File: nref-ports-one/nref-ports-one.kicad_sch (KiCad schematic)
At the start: 91 parts, among them J1 CONN_HEAD, J10 CONN_SPK, J2 DM3AT-SF-PEJM5, J3 09452812561, J4 USB_C_Receptacle, J5 Conn_01x10_Pin, J6 Conn_01x14_Pin, J7 Conn_01x12_Pin, J8 PWR, J9 Conn_01x10_Pin, U1 TPS7A0533PDBZ, U2 TLV320AIC3100, U3 TXS0108EPW, U4 SN74AVC1T45, U5 TPD4E02B04DQA, U6 TPD4E02B04DQA, U7 TPD4E02B04DQA, U8 FUSB302BMPX, U9 AP22815A

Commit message: ports one: some routing
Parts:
- removed FB5, FB6: 100@100MHz 3A, Inductor_SMD:L_0603_1608Metric, symbol Device:FerriteBead_Small
- C25: footprint Capacitor_SMD:C_0603_1608Metric -> Capacitor_SMD:C_0402_1005Metric
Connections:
- net GND: no longer J8.1 (Pin_1), J8.2 (Pin_2)
- net GNDA: no longer C24.1, C25.2, J10.2 (Pin_2), L2.2
- new net: C24.1, C25.2, J10.2 (Pin_2), L2.2
- new net VCC: J8.1 (Pin_1), J8.2 (Pin_2)
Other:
- note added: "TODO"
- moved on the sheet: C23, C24

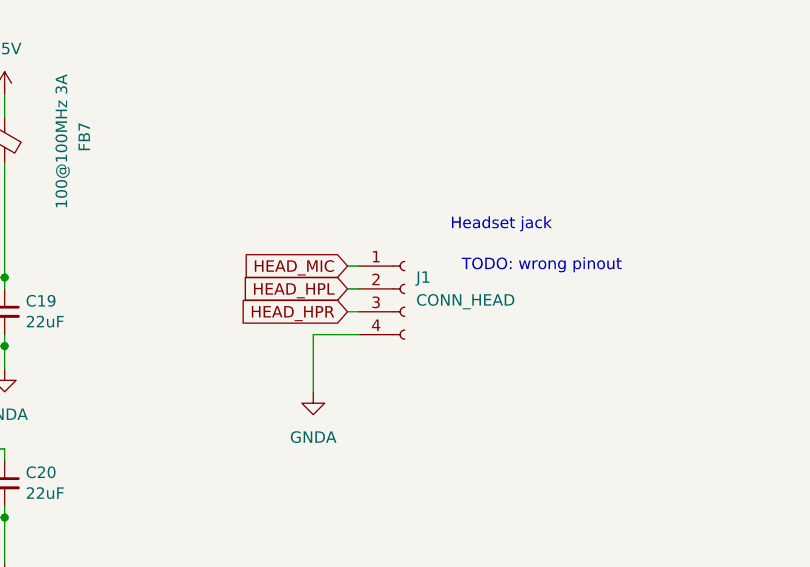
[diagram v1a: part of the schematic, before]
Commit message: ports 1 routing, ports 2 location tweaks
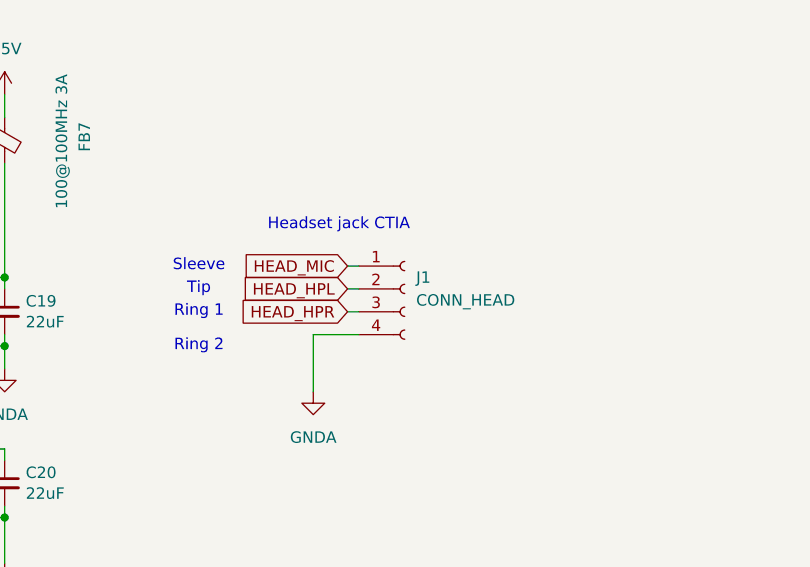
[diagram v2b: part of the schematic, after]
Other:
- note added: "Headset jack CTIA"
- note added: "Ring 1"
- note added: "Ring 2"
- note added: "Sleeve"
- note added: "Tip"
- note removed: "Headset jack"
- note removed: "TODO: wrong pinout"
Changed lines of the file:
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@@
-		)
-	)
-	(text "TODO: wrong pinout"
-		(exclude_from_sim no)
-		(at 198.12 393.7 0)
-		(effects
-			(font
-				(size 1.27 1.27)
-			)
 		)
 	)
@@
 		)
 	)
+	(text "Ring 1"
+		(exclude_from_sim no)
+		(at 160.02 398.78 0)
+		(effects
+			(font
+				(size 1.27 1.27)
+			)
+		)
+	)
 	(text "Audio"
 		(exclude_from_sim no)
@@
 			)
 			(justify left bottom)
+		)
+	)
+	(text "Sleeve"
+		(exclude_from_sim no)
+		(at 160.02 393.7 0)
+		(effects
+			(font
+				(size 1.27 1.27)
+			)
 		)
 	)
@@
 		)
 	)
-	(text "Headset jack"
+	(text "Headset jack CTIA"
 		(exclude_from_sim no)
-		(at 187.96 389.89 0)
+		(at 167.64 389.89 0)
 		(effects
 			(font
@@
 			)
 			(justify left bottom)
+		)
+	)
+	(text "Tip"
+		(exclude_from_sim no)
+		(at 160.02 396.24 0)
+		(effects
+			(font
+				(size 1.27 1.27)
+			)
 		)
 	)
@@
 		)
 	)
+	(text "Ring 2"
+		(exclude_from_sim no)
+		(at 160.02 402.59 0)
+		(effects
+			(font
+				(size 1.27 1.27)
+			)
+		)
+	)

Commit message: ports one: more design and more routing
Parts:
- added C38, C39, C40: 47uF, Capacitor_SMD:C_1206_3216Metric, symbol Device:C_Small
- added C41, C42: 0.1uF, Capacitor_SMD:C_0402_1005Metric, symbol Device:C_Small
- added C43, C44: 1uF, Capacitor_SMD:C_0402_1005Metric, symbol Device:C_Small
- added R20, R21, R22, R24, R31, R32, R33: 0, Resistor_SMD:R_0402_1005Metric, symbol Device:R_Small
- added R23, R25, R26, R27, R30: 200k, Resistor_SMD:R_0402_1005Metric, symbol Device:R_Small
- added R28, R34: 10k, Resistor_SMD:R_0402_1005Metric, symbol Device:R_Small
- added R29: 900k, Resistor_SMD:R_0402_1005Metric, symbol Device:R_Small
- added U10: HD3SS3220IRNHT, footprints:QFN40P450X250X80-31N120X320, symbol HD3SS3220IRNHT:HD3SS3220IRNHT
- added U11: PCAL6416AHF, Package_DFN_QFN:HVQFN-24-1EP_4x4mm_P0.5mm_EP2.1x2.1mm, symbol Interface_Expansion:PCAL6416AHF
- added U12: TLV75518PDBV, Package_TO_SOT_SMD:SOT-23-5, symbol Regulator_Linear:TLV75518PDBV
- J1: footprint (none) -> footprints:CUI_SJ-43614-SMT
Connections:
- net USBH_2_DN is gone; now on net USB1_DN: J4.A7 (D-), J4.B7 (D-), U5.4 (IO3), U5.7 (IO3)
- net USBH_2_DP is gone; now on net USB1_DP: J4.A6 (D+), J4.B6 (D+), U5.5 (IO4), U5.6 (IO4)
- net VCHG is gone; now on net VPD: D3.1 (K)
- net +1V8: now also C44.1, U12.5 (OUT)
- net +3V3: now also C43.1, R22.2, U12.1 (IN), U12.3 (EN)
- net +5V: now also R24.2
- net GND: now also C38.2, C39.2, C40.2, C41.2, C42.2, C43.2, C44.2, R31.1, U10.13 (GND), U10.22 (ADDR), U10.28 (GND), U10.29 (~{ENN_CC}), U10.31 (EXP_PAD), U11.18 (ADDR), U11.25 (EP), U11.9 (V_{SS}), U12.2 (GND)
- net RP_FUSB_INT: now also U11.8 (P0_7)
- net RP_SCL0: now also R32.2, U11.19 (SCL)
- net RP_SDA0: now also R33.2, U11.20 (SDA)
- net STANDBY_3V3: now also C41.1, R34.1, U11.21 (V_{DD(P)}), U11.23 (V_{DD(I2C-bus)})
- net USB1_RXN: now also U10.10 (RXN)
- net USB1_RXP: now also U10.9 (RXP)
- net USB1_TXN: now also U10.7 (TXN)
- net USB1_TXP: now also U10.6 (TXP)
- net USBH_2A_RXN: now also U10.14 (RX1N)
- net USBH_2A_RXP: now also U10.15 (RX1P)
- net USBH_2A_TXN: now also U10.16 (TX1N)
- net USBH_2A_TXP: now also U10.17 (TX1P)
- net USBH_2B_RXN: now also U10.18 (RX2N)
- net USBH_2B_RXP: now also U10.19 (RX2P)
- net USBH_2B_TXN: now also U10.20 (TX2N)
- net USBH_2B_TXP: now also U10.21 (TX2P)
- net USB_SRC_EN: now also U11.1 (P0_0)
- net USB_VBUS: now also C39.1, C40.1, R29.1, R30.1
- net CC1: now reaches J4.A5 (CC1), R18.1, U5.1 (IO1), U5.10 (IO1)
- net CC1: now also R21.1
- net CC2: now reaches J4.B5 (CC2), R17.1, U5.2 (IO2), U5.9 (IO2)
- net CC2: now also R20.1
- new net: R25.1, U10.27 (ID)
- new net: R23.1, U10.11 (DIR)
- new net: R30.2, U10.4 (PORT)
- new net: R26.1, U10.23 (~{INT_N}/OUT3)
- new net: R31.2, U10.12 (~{ENN_MUX})
- new net: R28.2, U10.3 (CURRENT_MODE)
- new net: R20.2, U10.1 (CC2)
- new net: R21.2, U10.2 (CC1)
- new net: R27.1, U10.24 (VCONN_FAULT_N)
- new net: R33.1, U10.25 (SDA/OUT1)
- new net: R32.1, U10.26 (SCL/OUT2)
- new net: R29.2, U10.5 (VBUS_DET)
- new net: R34.2, U11.24 (~{RESET})
- new net MUX_3V3: C42.1, R22.1, R23.2, U10.8 (VCC33)
- new net MUX_5V: C38.1, R24.1, R25.2, R26.2, R27.2, R28.1, U10.30 (VDD5)
- no-connect marks 13 -> 28
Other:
- note added: "GPIO bank controlled via I2C"
- note added: "LOL?"
- note added: "TODO: VCONN?"
- note added: "TODO: backflow possible from standby to 3v3?"
- note added: "TODO: can put status LEDs here"
- note added: "TODO: double check ENN_CC, PORT"
- note added: "TODO: possibly DNP"
- note added: "To charger on motherboard (SINK)"
- note added: "https://www.ti.com/lit/ds/symlink/hd3ss3220.pdf?ts=1718344395887"
- note removed: "TODO"
- note removed: "TODO: gpio expander"
- note removed: "To charger (SINK)"
- moved on the sheet: C10, C11, C12, C13, C14, C15, C16, C17, C18, C19, C20, C21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

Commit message: ports-one snapshot
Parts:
- added H1: MountingHole, MountingHole:MountingHole_2.2mm_M2, symbol Mechanical:MountingHole
- added H2: MountingHole_Pad, MountingHole:MountingHole_2.2mm_M2_Pad, symbol Mechanical:MountingHole_Pad
- added H3: BADGE, footprints:nref-ports-one-badge, symbol Mechanical:MountingHole
- added R35: 0, Resistor_SMD:R_0402_1005Metric, symbol Device:R_Small
- J2: footprint footprints:DM3AT-SF-PEJM5 -> Connector_Card:microSD_HC_Hirose_DM3AT-SF-PEJM5; symbol Connector:Micro_SD_Card_Det -> Connector:Micro_SD_Card_Det_Hirose_DM3AT
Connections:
- net GND: now also J2.10 (DET_A), J2.11 (SHIELD), H2.1, R35.1; no longer J2.P1 (SHIELD), J2.P2 (SHIELD), J2.P3 (SHIELD), J2.P4 (SHIELD), J2.SWA (DET_A), U10.29 (~{ENN_CC})
- net SD_DET: now also J2.9 (DET_B); no longer J2.SWB (DET_B)
- new net: R35.2, U10.29 (~{ENN_CC})
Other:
- note added: "GNDA area"
- note added: "TODO: useful for low level peripherals?"
- note removed: "LOL?"
- note removed: "TODO: can put status LEDs here"

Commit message: batterypack and ports one snapshot
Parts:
- C1: Manufacturer_No (none) -> 0402YA102JAT2A
- C17, C21: Manufacturer Murata -> TDK; Manufacturer_No GRM31CR61A476ME15L -> C3216X5R1E476M160AC
- C22, FB2, H1, H2, H3: now not fitted
- C38, C39, C40: Manufacturer (none) -> TDK; Manufacturer_No (none) -> C3216X5R1E476M160AC
- C43, C44: Manufacturer Samsung -> Yageo; Manufacturer_No CL05B104KO5NNNC -> CC0402KRX5R6BB105
- D3: Manufacturer MDD -> Panjit; Manufacturer_No SS54 -> SB54AFC-AU_R1_000A1
- J1: Manufacturer (none) -> CUI; Manufacturer_No (none) -> SJ-43614-SMT
- J5, J9: Manufacturer (none) -> Hirose; Manufacturer_No (none) -> FH12-10S-0.5SH
- J6: Manufacturer (none) -> Hirose; Manufacturer_No (none) -> FH12-14S-0.5SH
- J7: Manufacturer (none) -> Hirose; Manufacturer_No (none) -> FH12-12S-0.5SH
- J8: Manufacturer HR(Joint Tech Elec) -> JST; Manufacturer_No A2001WR-S-09PD01 -> SM09B-SRSS-TB
- R14, R19: Manufacturer_No RC0402FR-0710KL -> RC0402FR-7D10KL
- R23, R25, R26, R27, R30: Manufacturer Panasonic -> Bourns; Manufacturer_No ERJ2GE0R00X -> CR0402-JW-204GLF
- R28: Manufacturer Panasonic -> Yageo; Manufacturer_No ERJ2GE0R00X -> RC0402FR-7D10KL
- R29: value 900k -> 909k; Manufacturer Panasonic -> Bourns; Manufacturer_No ERJ2GE0R00X -> CR0402-FX-9093GLF
- R34: Manufacturer_No RC0402FR-07100KL -> RC0402FR-7D10KL
- TR1: Manufacturer Heling -> Pulse; Manufacturer_No MT24-S1T1 -> HX5084NLT
- U10: AVAILABILITY Good -> (none); Availability In Stock -> (none); Check_prices https://www.snapeda.com/parts/HD3SS3220IRNHT/Texas+Instrume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 -> (none); DESCRIPTION Super Speed Type-C DRP Port Controller USB 3.1 3.3V/5V T/R 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 -> (none); Description_1 10-Gbps USB 3.1 Type-C 2:1 mux with DRP Controller -> (none); MF Texas Instruments -> (none); MP HD3SS3220IRNHT -> (none); Manufacturer (none) -> Texas Instruments; Manufacturer_No (none) -> HD3SS3220IRNHT; PACKAGE WQFN-30 Texas Instruments -> (none); PART_REV C -> (none); PRICE 3.26 USD -> (none); Package WQFN-30 Texas Instruments -> (none); Price None -> (none); Purchase-URL https://www.snapeda.com/api/url_track_click_mouser/?unipart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 -> (none); STANDARD IPC-7351B -> (none); SnapEDA_Link https://www.snapeda.com/parts/HD3SS3220IRNHT/Texas+Instrume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 -> (none)
- U11: Manufacturer (none) -> NXP; Manufacturer_No (none) -> PCAL6416AHF,128
- U12: Manufacturer (none) -> Texas Instruments; Manufacturer_No (none) -> TLV75518PDBV
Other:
- note added: "TODO: these need larger footprints"

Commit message: add latest PCB updates
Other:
- note added: "TODO: pulldown missing on USB_SRC_EN!"
- note added: "TODO: resistor"
- moved on the sheet: H1, H2, H3, J5, J6, J7, J8, J9

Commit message: snapshot before merge
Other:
- note added: "TODO: 1uF input cap nominal"
- note added: "TODO: Clamp"
- note added: "TODO: VCONN"
- note removed: "TODO: VCONN?"
- moved on the sheet: C32, C41, D3, R19, R34, U11, U9

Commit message: add current notes on various schematics
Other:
- note added: "1GBe to motherboard"
- note added: "I2S Audio"
- note added: "SD Card"
- note added: "USB3 to port farm 1"
- note removed: "1GBe to motherboard (flipped)"
- note removed: "I2S Audio (flipped)"
- note removed: "SD Card (flipped)"
- note removed: "USB3 to port farm 1 (flipped)"
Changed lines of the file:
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@@
 		)
 	)
-	(text "1GBe to motherboard\n(flipped)"
+	(text "1GBe to motherboard"
 		(exclude_from_sim no)
 		(at 259.08 401.32 0)
@@
 		)
 	)
-	(text "SD Card\n(flipped)"
+	(text "SD Card"
 		(exclude_from_sim no)
 		(at 224.282 401.066 0)
@@
 		)
 	)
-	(text "I2S Audio\n(flipped)"
+	(text "I2S Audio"
 		(exclude_from_sim no)
 		(at 184.912 401.32 0)
@@
 		)
 	)
-	(text "USB3 to port farm 1\n(flipped)"
+	(text "USB3 to port farm 1"
 		(exclude_from_sim no)
 		(at 299.72 401.32 0)
